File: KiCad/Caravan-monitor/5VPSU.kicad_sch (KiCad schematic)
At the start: 15 parts, among them IC1 TPS54302DDCR

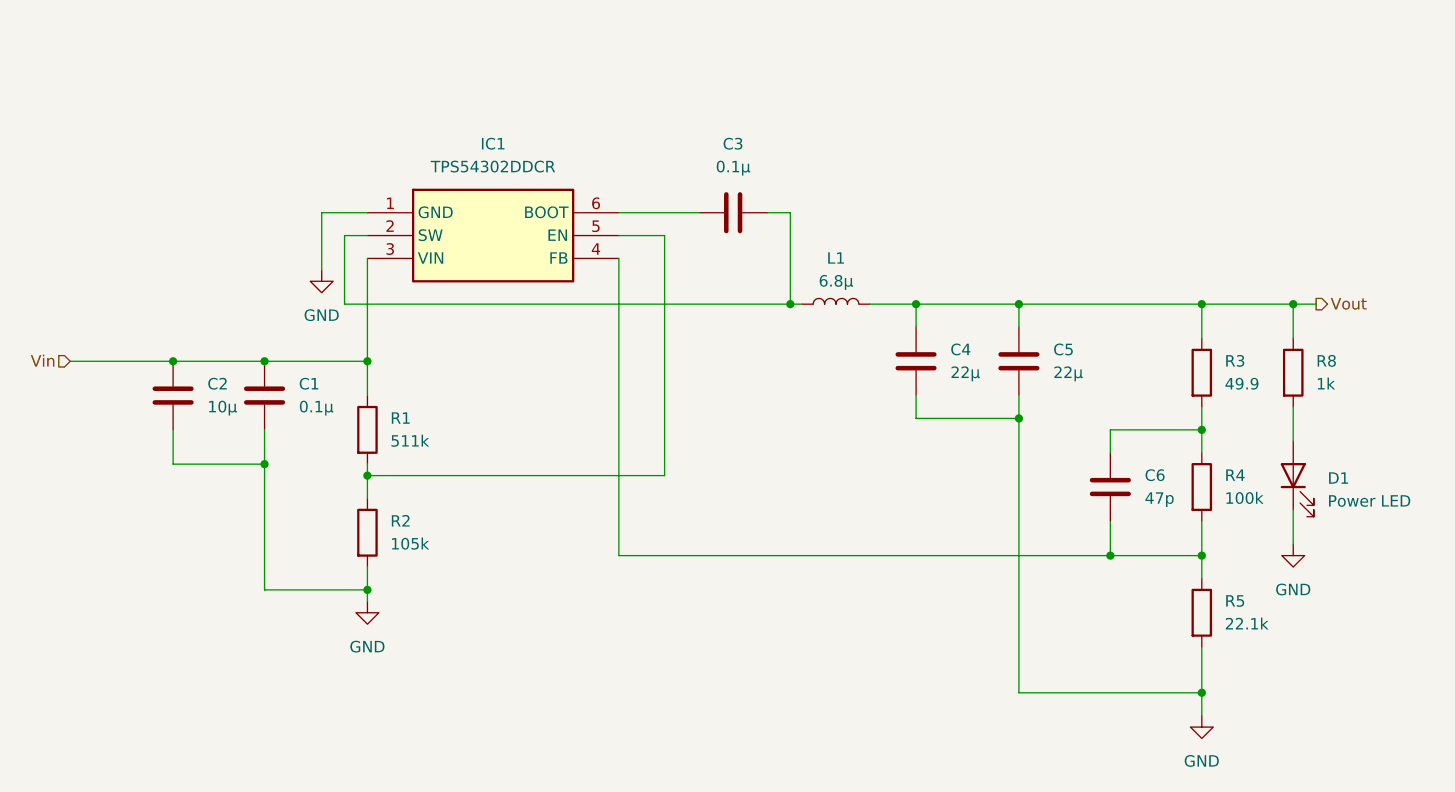
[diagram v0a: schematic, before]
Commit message: Battery voltage monitoring schematics
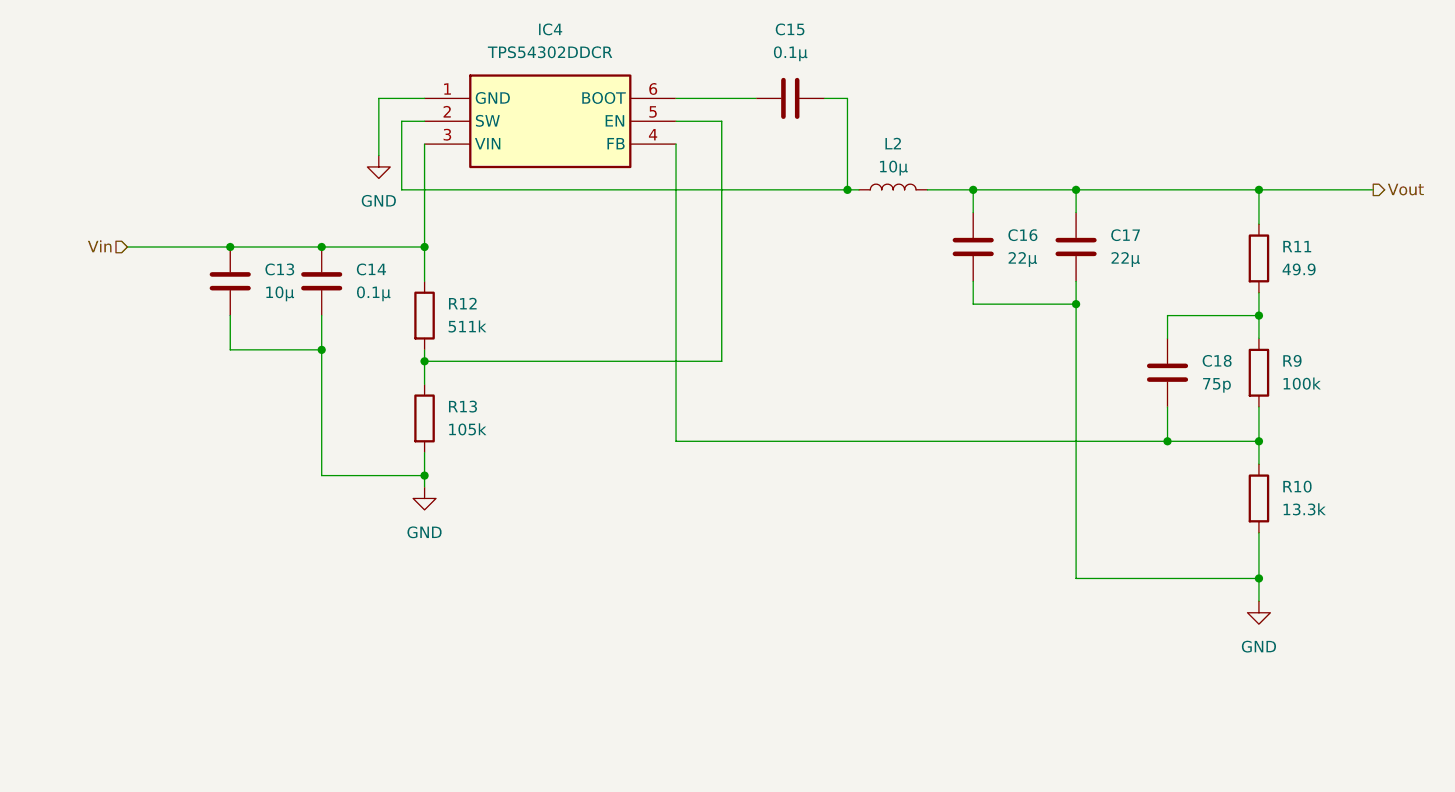
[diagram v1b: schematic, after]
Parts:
- removed C1, C3: 0.1µ, Capacitor_SMD:C_0805_2012Metric_Pad1.18x1.45mm_HandSolder, symbol Device:C
- removed C2: 10µ, Capacitor_SMD:C_0805_2012Metric_Pad1.18x1.45mm_HandSolder, symbol Device:C
- removed C4, C5: 22µ, Capacitor_SMD:C_0805_2012Metric_Pad1.18x1.45mm_HandSolder, symbol Device:C
- removed C6: 47p, Capacitor_SMD:C_0805_2012Metric_Pad1.18x1.45mm_HandSolder, symbol Device:C
- removed D1: Power LED, LED_SMD:LED_0805_2012Metric_Pad1.15x1.40mm_HandSolder, symbol Device:LED
- removed IC1: TPS54302DDCR, SamacSys_Parts:SOT95P280X110-6N, symbol SamacSys_Parts:TPS54302DDCR
- removed L1: 6.8µ, Inductor_SMD:L_0805_2012Metric_Pad1.05x1.20mm_HandSolder, symbol Device:L
- removed R1: 511k, Resistor_SMD:R_0805_2012Metric_Pad1.20x1.40mm_HandSolder, symbol Device:R
- removed R2: 105k, Resistor_SMD:R_0805_2012Metric_Pad1.20x1.40mm_HandSolder, symbol Device:R
- removed R3: 49.9, Resistor_SMD:R_0805_2012Metric_Pad1.20x1.40mm_HandSolder, symbol Device:R
- removed R4: 100k, Resistor_SMD:R_0805_2012Metric_Pad1.20x1.40mm_HandSolder, symbol Device:R
- removed R5: 22.1k, Resistor_SMD:R_0805_2012Metric_Pad1.20x1.40mm_HandSolder, symbol Device:R
- removed R8: 1k, Resistor_SMD:R_0805_2012Metric_Pad1.20x1.40mm_HandSolder, symbol Device:R
- added C13: 10µ, Capacitor_SMD:C_0805_2012Metric_Pad1.18x1.45mm_HandSolder, symbol Device:C
- added C14, C15: 0.1µ, Capacitor_SMD:C_0805_2012Metric_Pad1.18x1.45mm_HandSolder, symbol Device:C
- added C16, C17: 22µ, Capacitor_SMD:C_0805_2012Metric_Pad1.18x1.45mm_HandSolder, symbol Device:C
- added C18: 75p, Capacitor_SMD:C_0805_2012Metric_Pad1.18x1.45mm_HandSolder, symbol Device:C
- added IC4: TPS54302DDCR, SamacSys_Parts:SOT95P280X110-6N, symbol SamacSys_Parts:TPS54302DDCR
- added L2: 10µ, Inductor_SMD:L_0805_2012Metric_Pad1.05x1.20mm_HandSolder, symbol Device:L
- added R10: 13.3k, Resistor_SMD:R_0805_2012Metric_Pad1.20x1.40mm_HandSolder, symbol Device:R
- added R11: 49.9, Resistor_SMD:R_0805_2012Metric_Pad1.20x1.40mm_HandSolder, symbol Device:R
- added R12: 511k, Resistor_SMD:R_0805_2012Metric_Pad1.20x1.40mm_HandSolder, symbol Device:R
- added R13: 105k, Resistor_SMD:R_0805_2012Metric_Pad1.20x1.40mm_HandSolder, symbol Device:R
- added R9: 100k, Resistor_SMD:R_0805_2012Metric_Pad1.20x1.40mm_HandSolder, symbol Device:R
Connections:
- net GND: now also C13.2, C14.2, C16.2, C17.2, IC4.1 (GND), R10.2, R13.2
- net Vin: now also C13.1, C14.1, IC4.3 (VIN), R12.1
- net Vout: now also C16.1, C17.1, L2.2, R11.1
- new net: C18.1, R11.2, R9.1
- new net: C18.2, IC4.4 (FB), R10.1, R9.2
- new net: C15.2, IC4.2 (SW), L2.1
- new net: IC4.5 (EN), R12.2, R13.1
- new net: C15.1, IC4.6 (BOOT)

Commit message: Schematics done
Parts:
- C13, C14, C15, C16, C17, C18: footprint Capacitor_SMD:C_0805_2012Metric_Pad1.18x1.45mm_HandSolder -> Capacitor_SMD:C_0402_1005Metric_Pad0.74x0.62mm_HandSolder
- R10, R11, R12, R13, R9: footprint Resistor_SMD:R_0805_2012Metric_Pad1.20x1.40mm_HandSolder -> Resistor_SMD:R_0402_1005Metric_Pad0.72x0.64mm_HandSolder
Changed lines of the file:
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@@
 			)
 		)
-		(property "Footprint" "Resistor_SMD:R_0805_2012Metric_Pad1.20x1.40mm_HandSolder"
+		(property "Footprint" "Resistor_SMD:R_0402_1005Metric_Pad0.72x0.64mm_HandSolder"
 			(at 212.852 90.17 90)
 			(effects
@@
 			)
 		)
-		(property "Footprint" "Capacitor_SMD:C_0805_2012Metric_Pad1.18x1.45mm_HandSolder"
+		(property "Footprint" "Capacitor_SMD:C_0402_1005Metric_Pad0.74x0.62mm_HandSolder"
 			(at 101.2952 83.82 0)
 			(effects
@@
 			)
 		)
-		(property "Footprint" "Capacitor_SMD:C_0805_2012Metric_Pad1.18x1.45mm_HandSolder"
+		(property "Footprint" "Capacitor_SMD:C_0402_1005Metric_Pad0.74x0.62mm_HandSolder"
 			(at 183.8452 80.01 0)
 			(effects
@@
 			)
 		)
-		(property "Footprint" "Resistor_SMD:R_0805_2012Metric_Pad1.20x1.40mm_HandSolder"
+		(property "Footprint" "Resistor_SMD:R_0402_1005Metric_Pad0.72x0.64mm_HandSolder"
 			(at 120.142 95.25 90)
 			(effects
@@
 			)
 		)
-		(property "Footprint" "Resistor_SMD:R_0805_2012Metric_Pad1.20x1.40mm_HandSolder"
+		(property "Footprint" "Resistor_SMD:R_0402_1005Metric_Pad0.72x0.64mm_HandSolder"
 			(at 120.142 83.82 90)
 			(effects
@@
 			)
 		)
-		(property "Footprint" "Resistor_SMD:R_0805_2012Metric_Pad1.20x1.40mm_HandSolder"
+		(property "Footprint" "Resistor_SMD:R_0402_1005Metric_Pad0.72x0.64mm_HandSolder"
 			(at 212.852 77.47 90)
 			(effects
@@
 			)
 		)
-		(property "Footprint" "Resistor_SMD:R_0805_2012Metric_Pad1.20x1.40mm_HandSolder"
+		(property "Footprint" "Resistor_SMD:R_0402_1005Metric_Pad0.72x0.64mm_HandSolder"
 			(at 212.852 104.14 90)
 			(effects
@@
 			)
 		)
-		(property "Footprint" "Capacitor_SMD:C_0805_2012Metric_Pad1.18x1.45mm_HandSolder"
+		(property "Footprint" "Capacitor_SMD:C_0402_1005Metric_Pad0.74x0.62mm_HandSolder"
 			(at 205.4352 93.98 0)
 			(effects
@@
 			)
 		)
-		(property "Footprint" "Capacitor_SMD:C_0805_2012Metric_Pad1.18x1.45mm_HandSolder"
+		(property "Footprint" "Capacitor_SMD:C_0402_1005Metric_Pad0.74x0.62mm_HandSolder"
 			(at 111.4552 83.82 0)
 			(effects
@@
 			)
 		)
-		(property "Footprint" "Capacitor_SMD:C_0805_2012Metric_Pad1.18x1.45mm_HandSolder"
+		(property "Footprint" "Capacitor_SMD:C_0402_1005Metric_Pad0.74x0.62mm_HandSolder"
 			(at 195.2752 80.01 0)
 			(effects
@@
 			)
 		)
-		(property "Footprint" "Capacitor_SMD:C_0805_2012Metric_Pad1.18x1.45mm_HandSolder"
+		(property "Footprint" "Capacitor_SMD:C_0402_1005Metric_Pad0.74x0.62mm_HandSolder"
 			(at 166.37 58.7248 0)
 			(effects
